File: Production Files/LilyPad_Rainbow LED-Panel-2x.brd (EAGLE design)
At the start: 60.5 x 97 mm, 195 parts

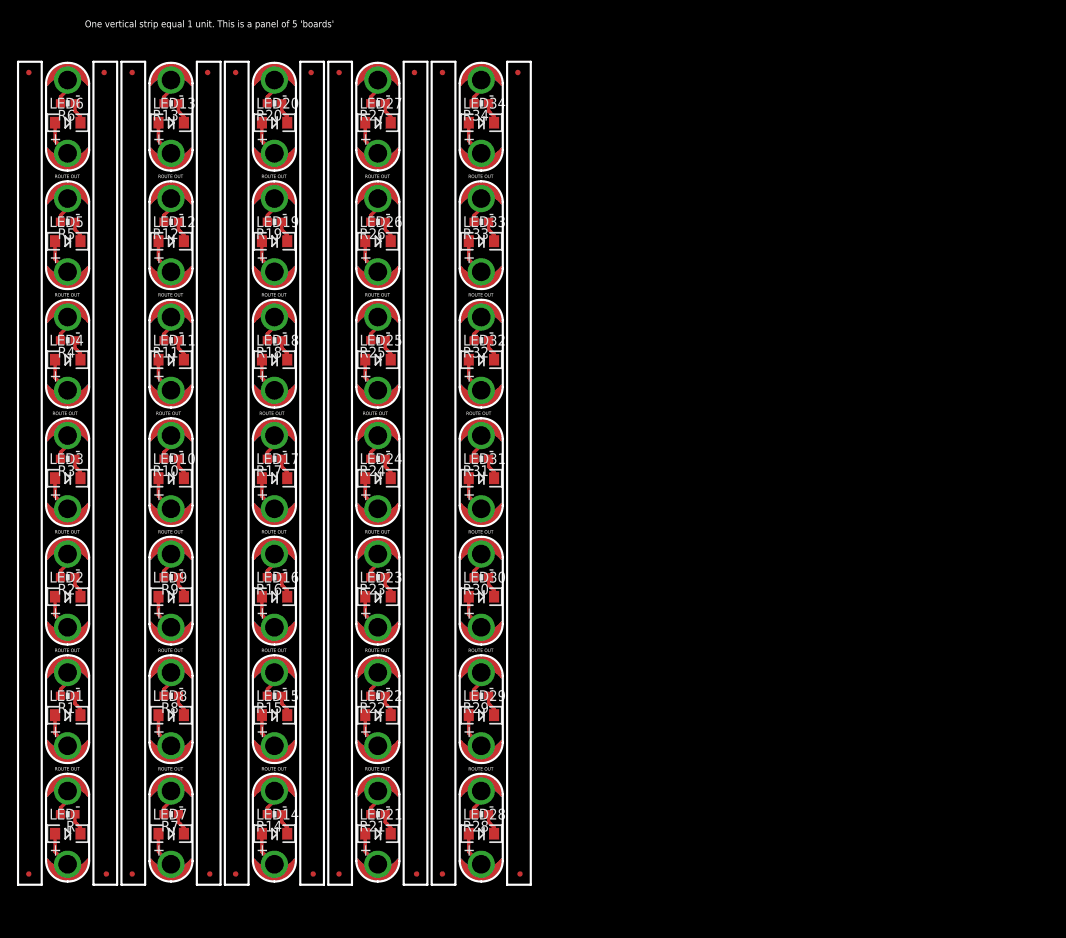
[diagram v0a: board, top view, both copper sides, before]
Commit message: v10 Production ready
added fiducials & doubled panel size.
added SFE flame logos to indicate where to cut the panel in half
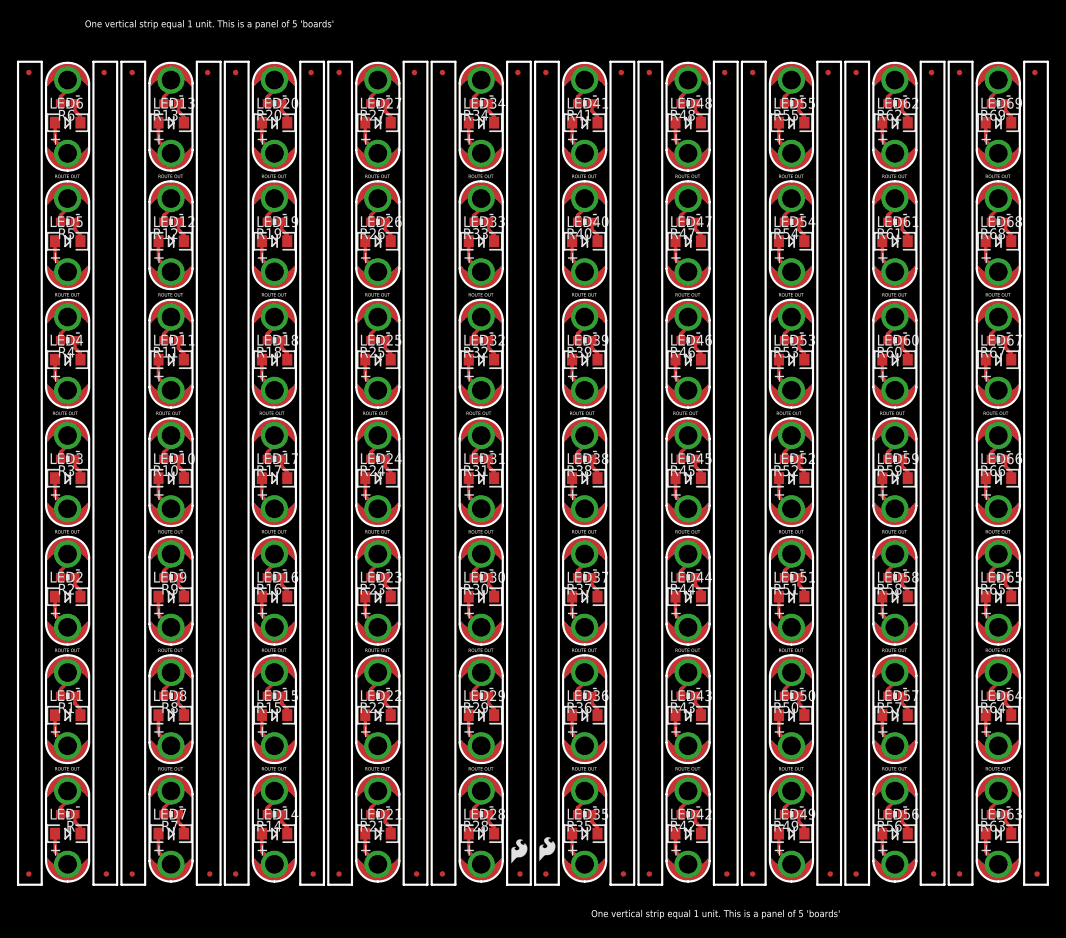
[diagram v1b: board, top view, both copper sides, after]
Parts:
- added E$21, E$22, E$23, E$24, E$25, E$26, E$27, E$28, E$29, E$30, E$31, E$32, E$33, E$34, E$35, E$36, E$37, E$38, E$39, E$40: (no value), SparkFun-Aesthetics:MICRO-FIDUCIAL
- added E$41, E$42: (no value), SparkFun-Aesthetics:SFE-LOGO-FLAME
- added LED+35, LED+36, LED+37, LED+38, LED+39, LED+40, LED+41, LED+42, LED+43, LED+44, LED+45, LED+46, LED+47, LED+48, LED+49, LED+50, LED+51, LED+52, LED+53, LED+54, LED+55, LED+56, LED+57, LED+58, LED+59, LED+60, LED+61, LED+62, LED+63, LED+64, LED+65, LED+66, LED+67, LED+68, LED+69, LED-35, LED-36, LED-37, LED-38, LED-39, LED-40, LED-41, LED-42, LED-43, LED-44, LED-45, LED-46, LED-47, LED-48, LED-49, LED-50, LED-51, LED-52, LED-53, LED-54, LED-55, LED-56, LED-57, LED-58, LED-59, LED-60, LED-61, LED-62, LED-63, LED-64, LED-65, LED-66, LED-67, LED-68, LED-69: SEWTAP6, LilyPad-Wearables:PETAL-SMALL
- added LED35, LED36, LED37, LED38, LED39, LED40, LED41, LED42, LED43, LED44, LED45, LED46, LED47, LED48, LED49, LED50, LED51, LED52, LED53, LED54, LED55, LED56, LED57, LED58, LED59, LED60, LED61, LED62, LED63, LED64, LED65, LED66, LED67, LED68, LED69: White, SparkFun-3-2-07:LED-1206
- added LOGO36, LOGO37, LOGO38, LOGO39, LOGO40, LOGO41, LOGO42, LOGO43, LOGO44, LOGO45, LOGO46, LOGO47, LOGO48, LOGO49, LOGO50, LOGO51, LOGO52, LOGO53, LOGO54, LOGO55, LOGO56, LOGO57, LOGO58, LOGO59, LOGO60, LOGO61, LOGO62, LOGO63, LOGO64, LOGO65, LOGO66, LOGO67, LOGO68, LOGO69, LOGO70: LOGO-LPL, LilyPad-Wearables:LOGO-L
- added R35, R36, R37, R38, R39, R40, R41, R42, R43, R44, R45, R46, R47, R48, R49, R50, R51, R52, R53, R54, R55, R56, R57, R58, R59, R60, R61, R62, R63, R64, R65, R66, R67, R68, R69: 100, SparkFun:0603-RES
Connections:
- new net +35: LED+35.1, LED35.A
- new net +36: LED+36.1, LED36.A
- new net +37: LED+37.1, LED37.A
- new net +38: LED+38.1, LED38.A
- new net +39: LED+39.1, LED39.A
- new net +40: LED+40.1, LED40.A
- new net +41: LED+41.1, LED41.A
- new net +42: LED+42.1, LED42.A
- new net +43: LED+43.1, LED43.A
- new net +44: LED+44.1, LED44.A
- new net +45: LED+45.1, LED45.A
- new net +46: LED+46.1, LED46.A
- new net +47: LED+47.1, LED47.A
- new net +48: LED+48.1, LED48.A
- new net +49: LED+49.1, LED49.A
- new net +50: LED+50.1, LED50.A
- new net +51: LED+51.1, LED51.A
- new net +52: LED+52.1, LED52.A
- new net +53: LED+53.1, LED53.A
- new net +54: LED+54.1, LED54.A
- new net +55: LED+55.1, LED55.A
- new net +56: LED+56.1, LED56.A
- new net +57: LED+57.1, LED57.A
- new net +58: LED+58.1, LED58.A
- new net +59: LED+59.1, LED59.A
- new net +60: LED+60.1, LED60.A
- new net +61: LED+61.1, LED61.A
- new net +62: LED+62.1, LED62.A
- new net +63: LED+63.1, LED63.A
- new net +64: LED+64.1, LED64.A
- new net +65: LED+65.1, LED65.A
- new net +66: LED+66.1, LED66.A
- new net +67: LED+67.1, LED67.A
- new net +68: LED+68.1, LED68.A
- new net +69: LED+69.1, LED69.A
- new net -35: LED-35.1, R35.2
- new net -36: LED-36.1, R36.2
- new net -37: LED-37.1, R37.2
- new net -38: LED-38.1, R38.2
- new net -39: LED-39.1, R39.2
- new net -40: LED-40.1, R40.2
- new net -41: LED-41.1, R41.2
- new net -42: LED-42.1, R42.2
- new net -43: LED-43.1, R43.2
- new net -44: LED-44.1, R44.2
- new net -45: LED-45.1, R45.2
- new net -46: LED-46.1, R46.2
- new net -47: LED-47.1, R47.2
- new net -48: LED-48.1, R48.2
- new net -49: LED-49.1, R49.2
- new net -50: LED-50.1, R50.2
- new net -51: LED-51.1, R51.2
- new net -52: LED-52.1, R52.2
- new net -53: LED-53.1, R53.2
- new net -54: LED-54.1, R54.2
- new net -55: LED-55.1, R55.2
- new net -56: LED-56.1, R56.2
- new net -57: LED-57.1, R57.2
- new net -58: LED-58.1, R58.2
- new net -59: LED-59.1, R59.2
- new net -60: LED-60.1, R60.2
- new net -61: LED-61.1, R61.2
- new net -62: LED-62.1, R62.2
- new net -63: LED-63.1, R63.2
- new net -64: LED-64.1, R64.2
- new net -65: LED-65.1, R65.2
- new net -66: LED-66.1, R66.2
- new net -67: LED-67.1, R67.2
- new net -68: LED-68.1, R68.2
- new net -69: LED-69.1, R69.2
- new net N$36: LED35.C, R35.1
- new net N$37: LED36.C, R36.1
- new net N$38: LED37.C, R37.1
- new net N$39: LED38.C, R38.1
- new net N$40: LED39.C, R39.1
- new net N$41: LED40.C, R40.1
- new net N$42: LED41.C, R41.1
- new net N$43: LED42.C, R42.1
- new net N$44: LED43.C, R43.1
- new net N$45: LED44.C, R44.1
- new net N$46: LED45.C, R45.1
- new net N$47: LED46.C, R46.1
- new net N$48: LED47.C, R47.1
- new net N$49: LED48.C, R48.1
- new net N$50: LED49.C, R49.1
- new net N$51: LED50.C, R50.1
- new net N$52: LED51.C, R51.1
- new net N$53: LED52.C, R52.1
- new net N$54: LED53.C, R53.1
- new net N$55: LED54.C, R54.1
- new net N$56: LED55.C, R55.1
- new net N$57: LED56.C, R56.1
- new net N$58: LED57.C, R57.1
- new net N$59: LED58.C, R58.1
- new net N$60: LED59.C, R59.1
- new net N$61: LED60.C, R60.1
- new net N$62: LED61.C, R61.1
- new net N$63: LED62.C, R62.1
- new net N$64: LED63.C, R63.1
- new net N$65: LED64.C, R64.1
- new net N$66: LED65.C, R65.1
- new net N$67: LED66.C, R66.1
- new net N$68: LED67.C, R67.1
- new net N$69: LED68.C, R68.1
- new net N$70: LED69.C, R69.1
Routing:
- net +58: track 0.00 -> 4.35 mm
- net +57: track 0.00 -> 4.35 mm
- net +44: track 0.00 -> 4.35 mm
- net +43: track 0.00 -> 4.35 mm
- net +37: track 0.00 -> 4.35 mm
- net +36: track 0.00 -> 4.35 mm
- net +56: track 0.00 -> 4.35 mm
- net +42: track 0.00 -> 4.35 mm
- net +35: track 0.00 -> 4.35 mm
- net +60: track 0.00 -> 4.35 mm
- net +46: track 0.00 -> 4.35 mm
- net +39: track 0.00 -> 4.35 mm
- net +59: track 0.00 -> 4.35 mm
- net +45: track 0.00 -> 4.35 mm
- net +38: track 0.00 -> 4.35 mm
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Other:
- board size 60.5 x 97 mm -> 121.4 x 97 mm
